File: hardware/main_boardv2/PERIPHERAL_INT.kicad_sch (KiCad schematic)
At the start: 11 parts, among them IC401 PI4IOE5V9537UEX, J401 1x8 Male Pins, J402 2x5 Socket Pins

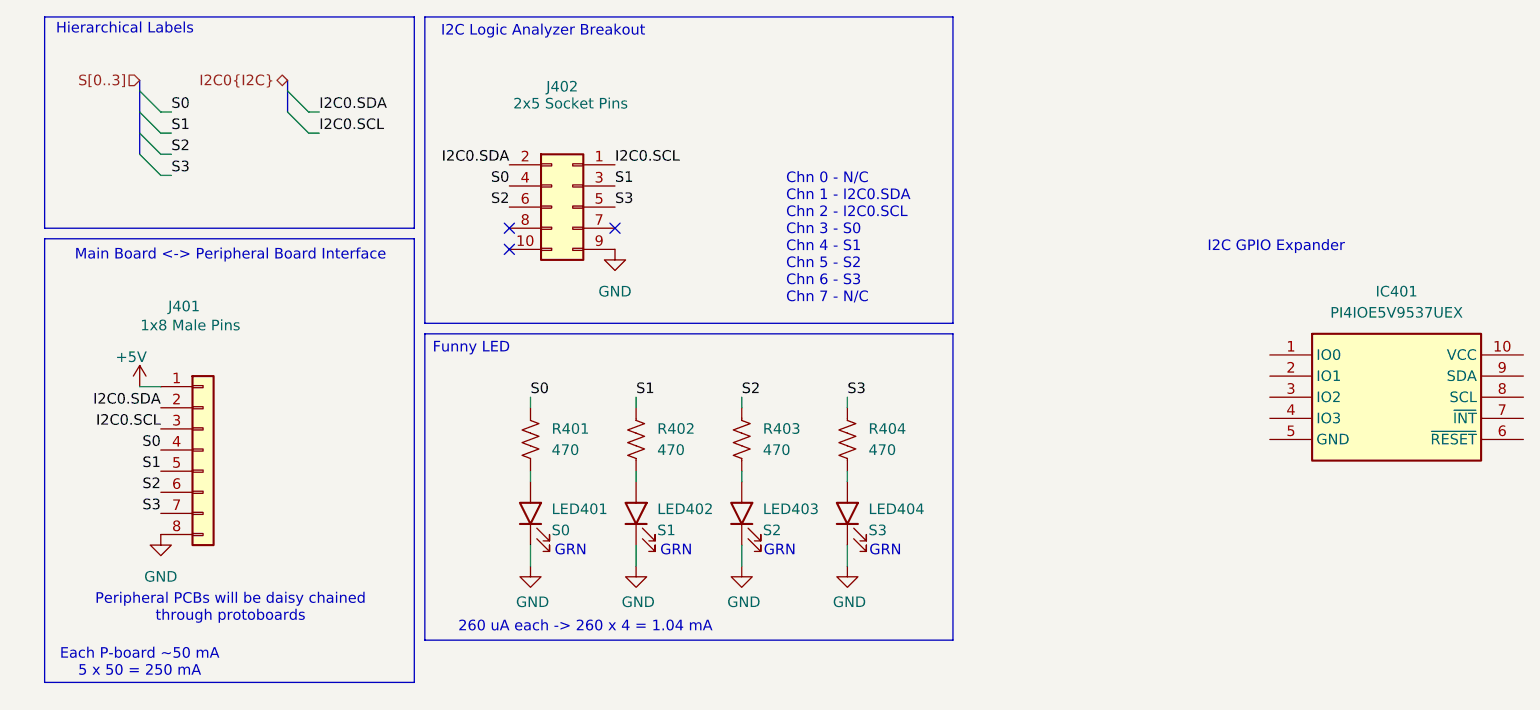
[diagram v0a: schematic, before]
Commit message: wired most of new hardware. need to reviist audio stuff
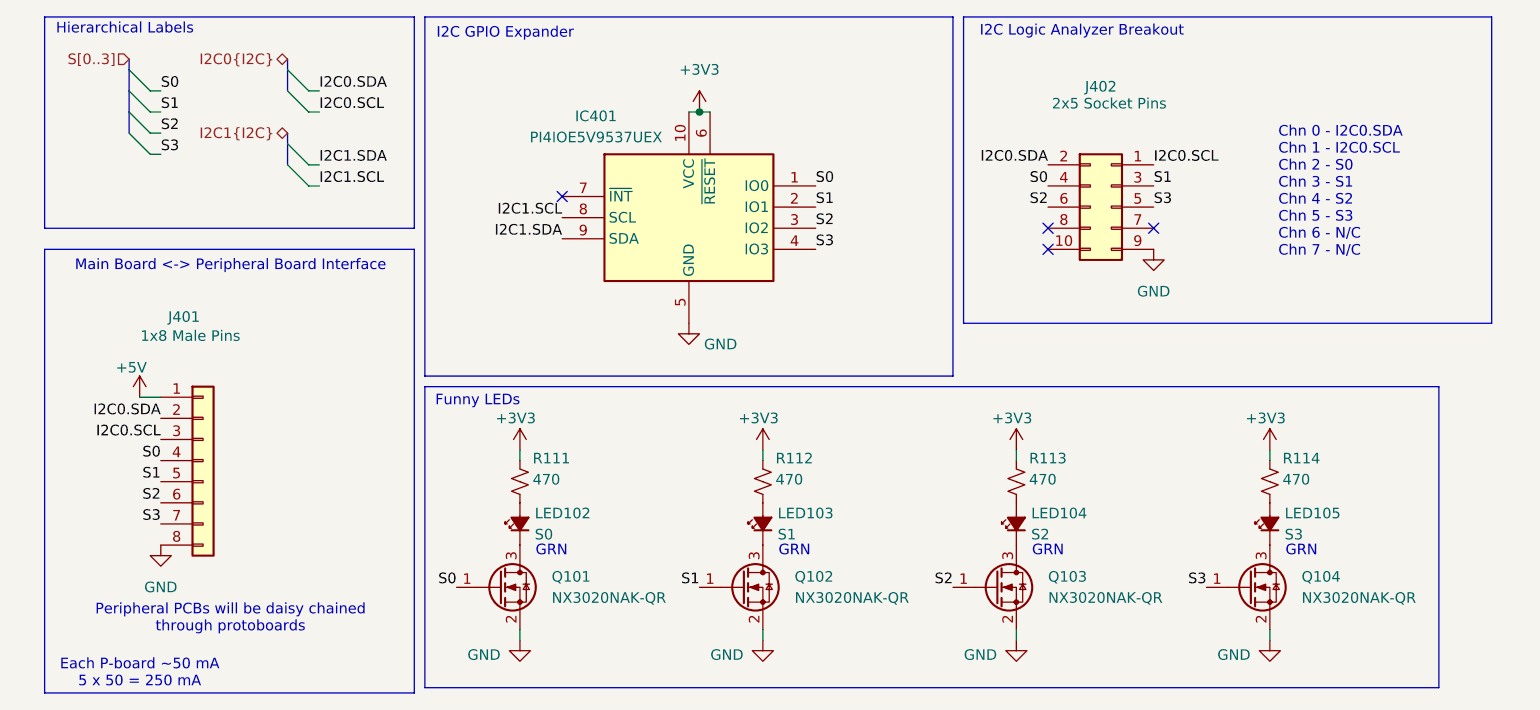
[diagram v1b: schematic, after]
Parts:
- removed LED401: S0, SamacSys_Parts:LEDC2012X40N, symbol ECE445L:LED
- removed LED402: S1, SamacSys_Parts:LEDC2012X40N, symbol ECE445L:LED
- removed LED403: S2, SamacSys_Parts:LEDC2012X40N, symbol ECE445L:LED
- removed LED404: S3, SamacSys_Parts:LEDC2012X40N, symbol ECE445L:LED
- removed R401, R402, R403, R404: 470, Resistor_SMD:R_0805_2012Metric, symbol Device:R_US
- added LED102: S0, SamacSys_Parts:LEDC2012X40N, symbol Device:LED_Small_Filled
- added LED103: S1, SamacSys_Parts:LEDC2012X40N, symbol Device:LED_Small_Filled
- added LED104: S2, SamacSys_Parts:LEDC2012X40N, symbol Device:LED_Small_Filled
- added LED105: S3, SamacSys_Parts:LEDC2012X40N, symbol Device:LED_Small_Filled
- added Q101, Q102, Q103, Q104: NX3020NAK-QR, SamacSys_Parts:SOT95P230X110-3N, symbol Transistor_FET:Q_NMOS_GSD
- added R111, R112, R113, R114: 470, Resistor_SMD:R_0805_2012Metric, symbol Device:R_Small_US
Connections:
- net GND: now also IC401.5 (GND), Q101.2 (S), Q102.2 (S), Q103.2 (S), Q104.2 (S)
- net S0: now also IC401.1 (IO0), Q101.1 (G)
- net S1: now also IC401.2 (IO1), Q102.1 (G)
- net S2: now also IC401.3 (IO2), Q103.1 (G)
- net S3: now also IC401.4 (IO3), Q104.1 (G)
- net +3V3: now reaches IC401.10 (VCC)
- net +3V3: now also IC401.6 (~{RESET}), R111.2, R112.2, R113.2, R114.2
- net I2C1.SCL: now reaches IC401.8 (SCL)
- net I2C1.SDA: now reaches IC401.9 (SDA)
- new net: LED102.1 (K), Q101.3 (D)
- new net: LED105.1 (K), Q104.3 (D)
- new net: LED105.2 (A), R114.1
- new net: LED102.2 (A), R111.1
- new net: LED104.2 (A), R113.1
- new net: LED103.1 (K), Q102.3 (D)
- new net: LED103.2 (A), R112.1
- new net: LED104.1 (K), Q103.3 (D)
- no-connect marks 3 -> 4
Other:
- note added: "Chn 0 - I2C0.SDA Chn 1 - I2C0.SCL Chn 2 - S0 Chn 3 - S1 Chn 4 - S2 Chn 5 - S3 Chn 6 - N/C Chn 7 - N/C"
- note added: "Funny LEDs"
- note removed: "260 uA each -> 260 x 4 = 1.04 mA"
- note removed: "Chn 0 - N/C Chn 1 - I2C0.SDA Chn 2 - I2C0.SCL Chn 3 - S0 Chn 4 - S1 Chn 5 - S2 Chn 6 - S3 Chn 7 - N/C"
- note removed: "Funny LED"
- moved on the sheet: IC401, J401, J402
